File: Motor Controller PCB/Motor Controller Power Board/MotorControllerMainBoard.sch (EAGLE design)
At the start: 96 parts, among them T1 TEENSY_3.1_ALL_PINS

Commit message: Started Power Board, added optoisolator
Cleaned up the schematic. Found an optoisolater to replace the original FET driver.
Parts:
- removed AD8512ARZ: TL072CDT, MotorControllerEagleLibrary:TL072CDT
- removed C13, C15, C47, C49: 100uf, SparkFun-Capacitors:CAP_POLC
- removed C14, C16, C48, C50: 10uf, resistor:C-EUC0805
- removed C17, C22: 1uf, resistor:C-EUC0805
- removed C18, C21: 0.1uf, resistor:C-EUC0805
- removed C23, C25, C46: 1uF, rcl:C-EUC0805
- removed C51, C52, C53, C55, C56, C57, C59, C60: 10uF, resistor:C-EUC0805
- removed D1, D2: BAT20J, SparkFun-DiscreteSemi:DIODE-SCHOTTKY-BAT20J
- removed D3, D4: 16V, SparkFun-DiscreteSemi:DIODE-ZENER16V
- removed ENCODER_INPUT: 90130-106, con-molex-c-grid:90130-106
- removed J1: (no value), SparkFun-Connectors:M04PTH
- removed J2: (no value), SparkFun-Connectors:M04X2
- removed J3: (no value), SparkFun-Connectors:M03PTH
- removed L2: 42nH, SparkFun (2015_10_14 22_27_04 UTC):INDUCTOR0805
- removed MIC4452: MIC4420M, transistor-power:MIC4420M
- removed O1: OPENLOG, openlog:OPENLOG
- removed R13, R14, R6, R7: 4.7k, SparkFun-Passives:RESISTOR0805-RES
- removed R15, R16: 10k, SparkFun-Passives:RESISTOR0805-RES
- removed R2, R3, R4: 3.3k, resistor:R-US_R0805
- removed R5: 90.9k, rcl:R-US_R0805
- removed R8: 10k, rcl:R-US_R0805
- removed T1: TEENSY_3.1_ALL_PINS, Teensy_3_and_LC_Series_Boards_v1.1:TEENSY_3.1_ALL_PINS
- removed T2: (no value), zetex:NMOS2SO8
- U$17: value ICL7662CBA -> TLP5771; device linear:ICL7662CBA -> MotorControllerEagleLibrary:TLP5771
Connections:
- removed net BUTTON1: J2.5, R15.1, T1.3/CAN-TX/PWM
- removed net BUTTON2: J2.7, R16.1, T1.4/CAN-RX-PWM
- removed net COAST_ENABLE: T1.20/A6/PWM
- removed net CURRENT_FEEDBACK: AD8512ARZ.1IN-, AD8512ARZ.1OUT, C46.1, D2.C, D4.C, T1.14/A0
- removed net ENCODER_A: ENCODER_INPUT.1, R2.2, T1.15/A1/T
- removed net ENCODER_B: ENCODER_INPUT.3, R3.2, T1.16/A2/T
- removed net HALL: J3.3, T1.10/TX2/PWM
- removed net INDEX: ENCODER_INPUT.4, R4.2, T1.17/A3/T
- removed net N$14: C51.1, C52.1, C53.1, U$17.CAP+
- removed net N$15: C51.2, C52.2, C53.2, U$17.CAP-
- removed net N$19: J1.3, R7.1, T2B.D
- removed net N$20: J1.4, R6.1, T2A.D
- removed net N$9: C17.1, C18.1, L2.1, T1.AREF
- removed net OUTPUT_12NEG: AD8512ARZ.VCC-, C55.1, C56.1, C57.1, U$17.VOUT
- removed net RX1: O1.TXO, T1.0/RX1/T
- removed net RX3: J2.8, T1.7/RX3
- removed net SCL0: R14.1, T1.19/A5/T/SCL0, T2B.S
- removed net SDA0: R13.1, T1.18/A4/T/SDA0, T2A.S
- removed net SUPPLY_VOLTAGE: AD8512ARZ.2IN-, AD8512ARZ.2OUT, C25.1, D1.C, D3.C, T1.22/A8/T/PWM
- removed net TEENSY_FET_DRIVER_SIGNAL: MIC4452.IN, R1.2, T1.23/A9/T/PWM
- removed net TX1: O1.RXI, T1.1/TX1/T
- removed net TX3: J2.6, T1.8/TX3
- net 12V_POWER_REGULATED: now also U$17.6.VCC; no longer AD8512ARZ.VCC+, C59.1, C60.1, J2.3, MIC4452.VS, MIC4452.VS1, U$17.V+
- net 3.3V_POWER_REGULATED: no longer C15.+, C16.1, C49.+, C50.1, L2.2, O1.RAW, R13.2, R14.2, T1.3.3V, T2A.G, T2B.G
- net 5V_POWER_REGULATED: no longer C13.+, C14.1, C21.1, C22.1, C47.+, C48.1, ENCODER_INPUT.2, J1.2, J2.4, J3.2, R2.1, R3.1, R4.1, R6.2, R7.2, T1.VIN
- net CURRENT_SENSOR_OUTPUT: no longer AD8512ARZ.1IN+
- net FET_DRIVER_SIGNAL: now also U$17.5.VOUT; no longer MIC4452.OUT@1
- net GND: now also U$17.4.GND; no longer C13.-, C14.2, C15.-, C16.2, C17.2, C18.2, C21.2, C22.2, C23.2, C25.2, C46.2, C47.-, C48.2, C49.-, C50.2, C55.2, C56.2, C57.2, C59.2, C60.2, D1.A, D2.A, D3.A, D4.A, ENCODER_INPUT.5, ENCODER_INPUT.6, J1.1, J2.1, J2.2, J3.1, MIC4452.GND, MIC4452.GND1, O1.GND, O1.GND2, R15.2, R16.2, R8.1, T1.AGND, T1.GND, U$17.GND, U$17.LV, U$17.TEST
- net INPUT_POWER(+): no longer C23.1, R5.1
- net N$7: now also R1.2, U$17.3.CATHODE; no longer AD8512ARZ.2IN+, R5.2, R8.2
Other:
- note removed: "2OUT = .099*Vin"
- note removed: "Encoder Terminal"
- note removed: "For Future revision"
- note removed: "Hall Effect"
- note removed: "IO"
- note removed: "If a block becomes bloated with parts, make a new sheet. Keep this sheet nice and simple."
- note removed: "Relay Enable Coast"
- note removed: "Schottky"
- note removed: "TEENSY 3.2 CONNECTIONS"
- note removed: "Use TL032IDR OpAmp RB500V-40-TP Schottky BZT52C4V7-TP Zener Diode"
- note removed: "Zener"
- note removed: "i2c"

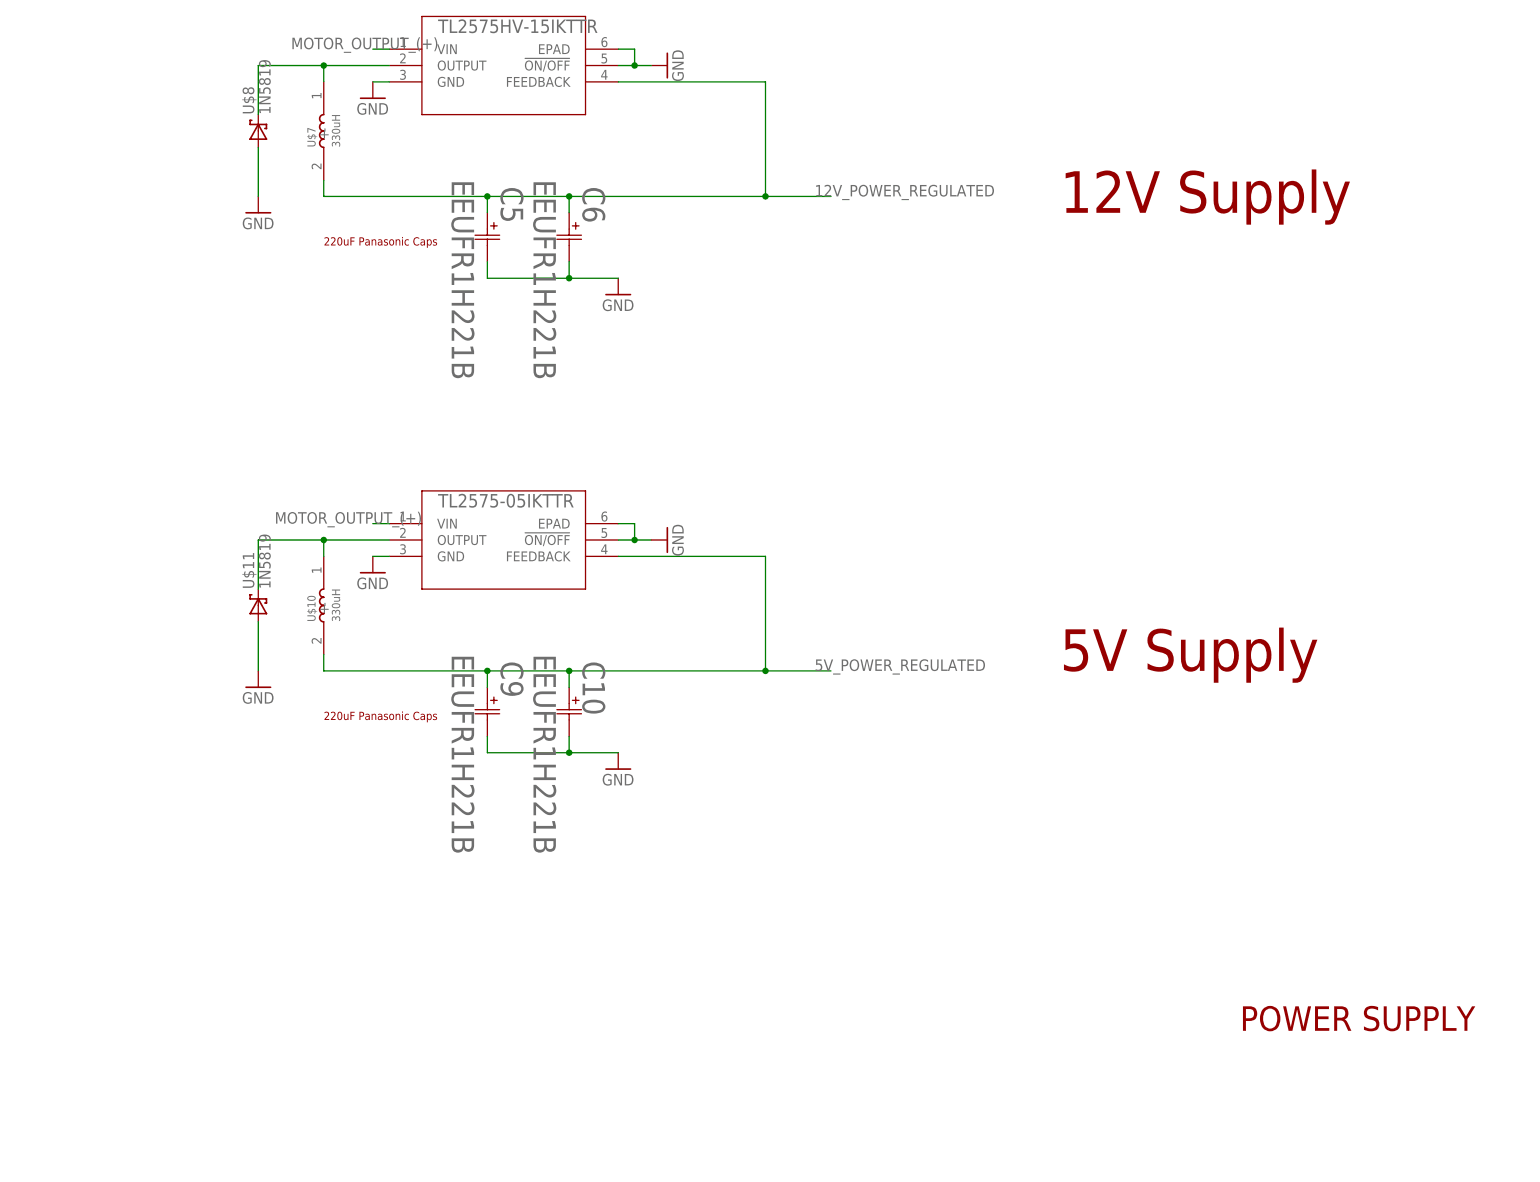
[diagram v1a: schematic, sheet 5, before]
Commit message: Added flyback transformer to library
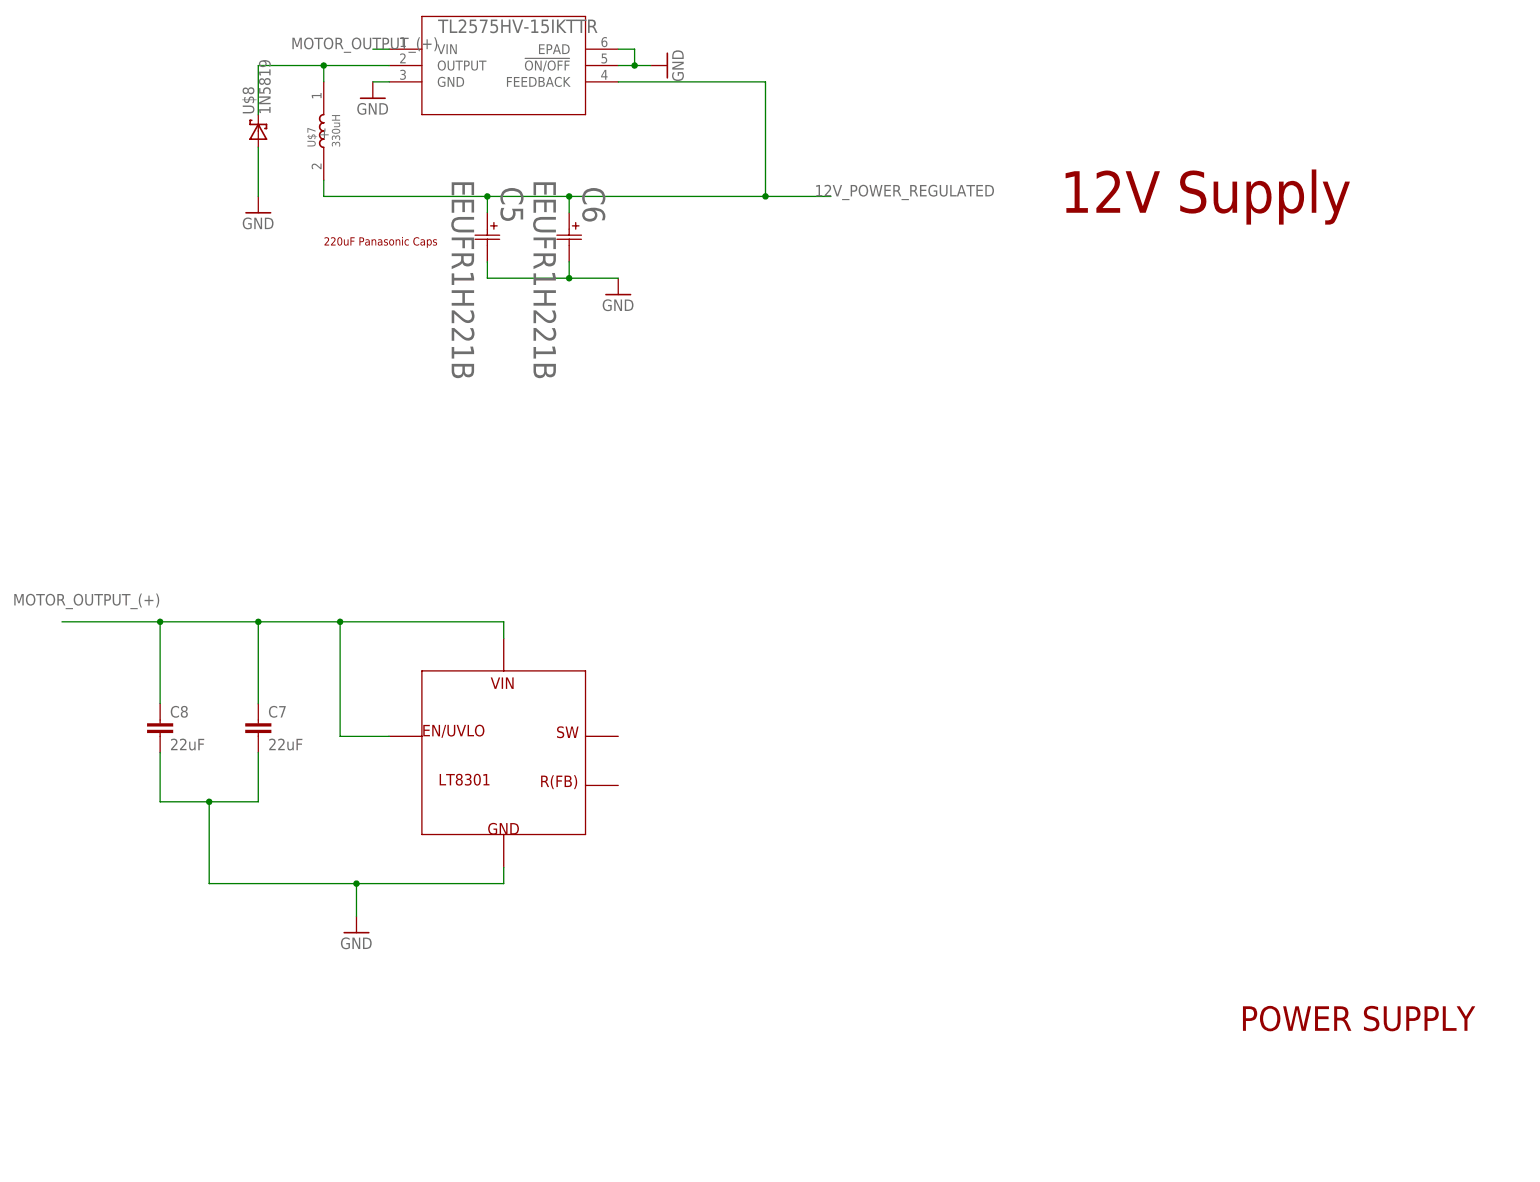
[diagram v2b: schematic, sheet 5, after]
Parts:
- removed C10, C9: EEUFR1H221B, MotorControllerEagleLibrary:EEUFR1H221B
- removed U$11: 1N5819, MotorControllerEagleLibrary:1N5819
- removed U$13: TL2575-05IKTTR, MotorControllerEagleLibrary:TL2575-05IKTTR
- added C7, C8: 22uF, rcl:C-EUC1210
- C1: device rcl:C-EUC1206 -> rcl:C-EUC1210
- C19: value 1uf -> 2.2uf
- C20: value 0.1uf -> 100nF
- U$10: value 330uH -> LT8301; device MotorControllerEagleLibrary:PA4320 -> MotorControllerEagleLibrary:LT8301
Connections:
- removed net 5V_POWER_REGULATED: C10.11, C9.11, U$10.-, U$13.FEEDBACK
- removed net N$4: U$10.+, U$11.K, U$13.OUTPUT
- net GND: now also C7.2, C8.2, U$10.GND; no longer C10.22, C9.22, U$11.A, U$13.!ON/OFF, U$13.EPAD, U$13.GND
- net MOTOR_OUTPUT_(+): now also C7.1, C8.1, U$10.EN/UVLO, U$10.VIN; no longer U$13.VIN
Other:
- note added: "This component needs to be spec'ed"
- note removed: "5V Supply"

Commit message: Minor Touches
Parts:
- removed C8: 22uF, rcl:C-EUC1210
- removed U$10: LT8301, MotorControllerEagleLibrary:LT8301
- C7: value 22uF -> EEUFR1H221B; device rcl:C-EUC1210 -> MotorControllerEagleLibrary:EEUFR1H221B
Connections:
- new net GND_ISOLATED: R1.1
- net 12V_POWER_REGULATED: now also C7.11
- net GND: now also C7.22; no longer C7.2, C8.2, R1.1, U$10.GND
- net MOTOR_OUTPUT_(+): no longer C7.1, C8.1, U$10.EN/UVLO, U$10.VIN
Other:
- note added: "4.7ohm Resistors on gates to nullify ringin, and to reduce peak currents"
- note removed: "4.7ohm Resistors on gates to nullify ringing."
- moved on the sheet: C5, C6, U$7, U$8

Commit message: Added opto-isolator amplifier
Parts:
- added U$10: AMC1200BDWVR, MotorControllerEagleLibrary:AMC1200BDWVR
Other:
- note removed: "Future Revision will have circuit protection in this block"
- note removed: "USING MIC4452YM-TR"
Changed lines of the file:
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@@
 <?xml version="1.0" encoding="utf-8"?>
 <!DOCTYPE eagle SYSTEM "eagle.dtd">
-<eagle version="8.5.2">
+<eagle version="8.4.0">
 <drawing>
 <settings>
@@
 <part name="GND9" library="E-P-008-R1.2" deviceset="GND" device=""/>
 <part name="C7" library="MotorControllerEagleLibrary" deviceset="EEUFR1H221B" device=""/>
+<part name="FRAME6" library="E-P-008-R1.2" deviceset="FRAME_A_L" device="" value="Voltage_FeedBack"/>
+<part name="U$10" library="MotorControllerEagleLibrary" deviceset="AMC1200BDWVR" device=""/>
 </parts>
 <sheets>
@@
 <text x="175.26" y="25.4" size="2.286" layer="94">Keep it looking neat. Use other sheets to make complicated circuits</text>
 <text x="20.32" y="58.42" size="1.778" layer="91">Terminal Block (Negative)</text>
-<text x="53.34" y="190.5" size="1.778" layer="91">Future Revision will have
-circuit protection in this block</text>
 </plain>
 <instances>
@@
 <plain>
 <text x="193.04" y="27.94" size="5.08" layer="94">MOSFET DRIVER</text>
-<text x="182.88" y="40.64" size="5.08" layer="94">USING MIC4452YM-TR</text>
 <text x="149.86" y="142.24" size="1.778" layer="94">All must be X7R</text>
 <text x="104.14" y="99.06" size="1.778" layer="92">This component
@@
 </nets>
 </sheet>
+<sheet>
+<description>Voltage FeedBack</description>
+<plain>
+</plain>
+<instances>
+<instance part="FRAME6" gate="G$1" x="0" y="0"/>
+<instance part="FRAME6" gate="G$2" x="172.72" y="0"/>
+<instance part="U$10" gate="A" x="139.7" y="116.84"/>
+</instances>
+<busses>
+</busses>
+<nets>
+</nets>
+</sheet>
 </sheets>
 </schematic>
@@
 packages will not be understood (or retained) with this version.
 </note>
-<note version="8.4" severity="warning">
-Since Version 8.4, EAGLE supports properties for SPICE simulation.
-Probes in schematics and SPICE mapping objects found in parts and library devices
-will not be understood with this version. Update EAGLE to the latest version
-for full support of SPICE simulation.
-</note>
 </compatibility>
